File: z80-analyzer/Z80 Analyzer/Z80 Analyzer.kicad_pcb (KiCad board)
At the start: 2 copper layers, 65 x 65 mm, 49 parts, among them J1 Conn_01x40_Pin, M1 TestPoint, U1 Z80CPU

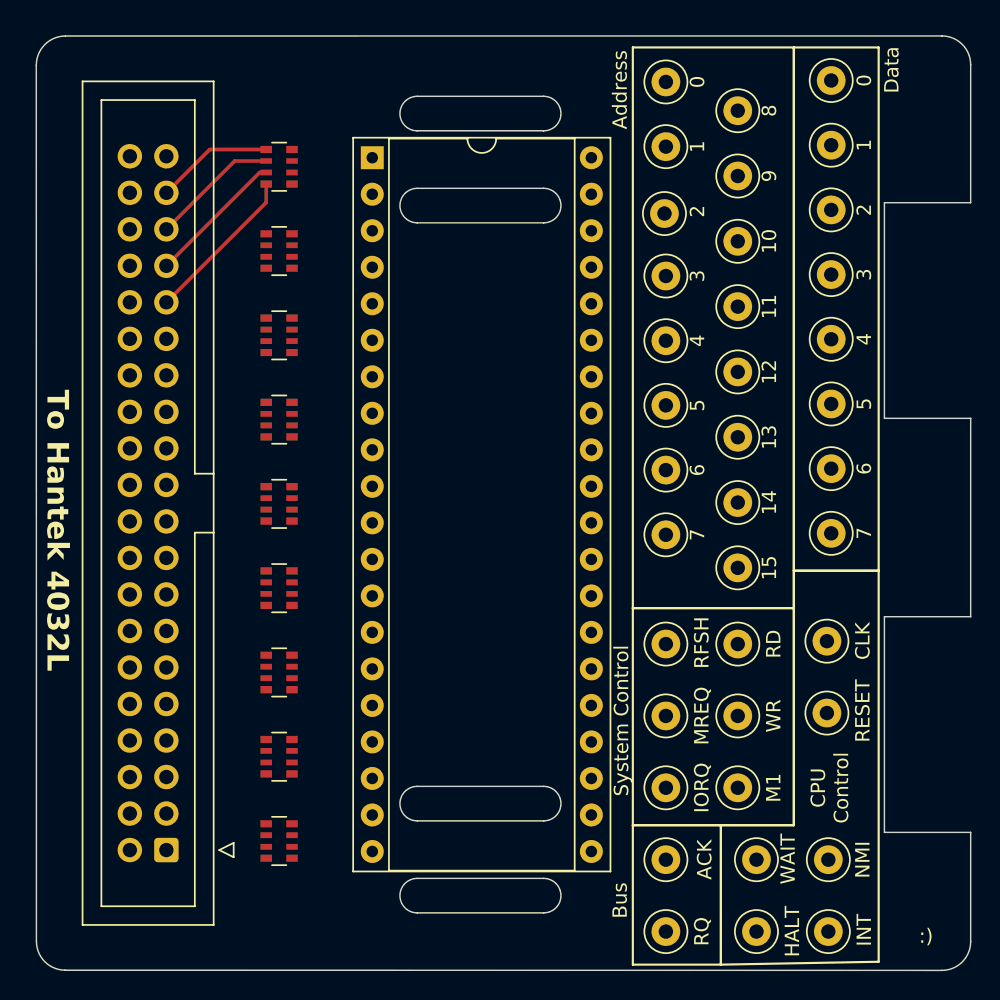
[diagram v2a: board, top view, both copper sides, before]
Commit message: [Z80] New routing, just needs rechecking now
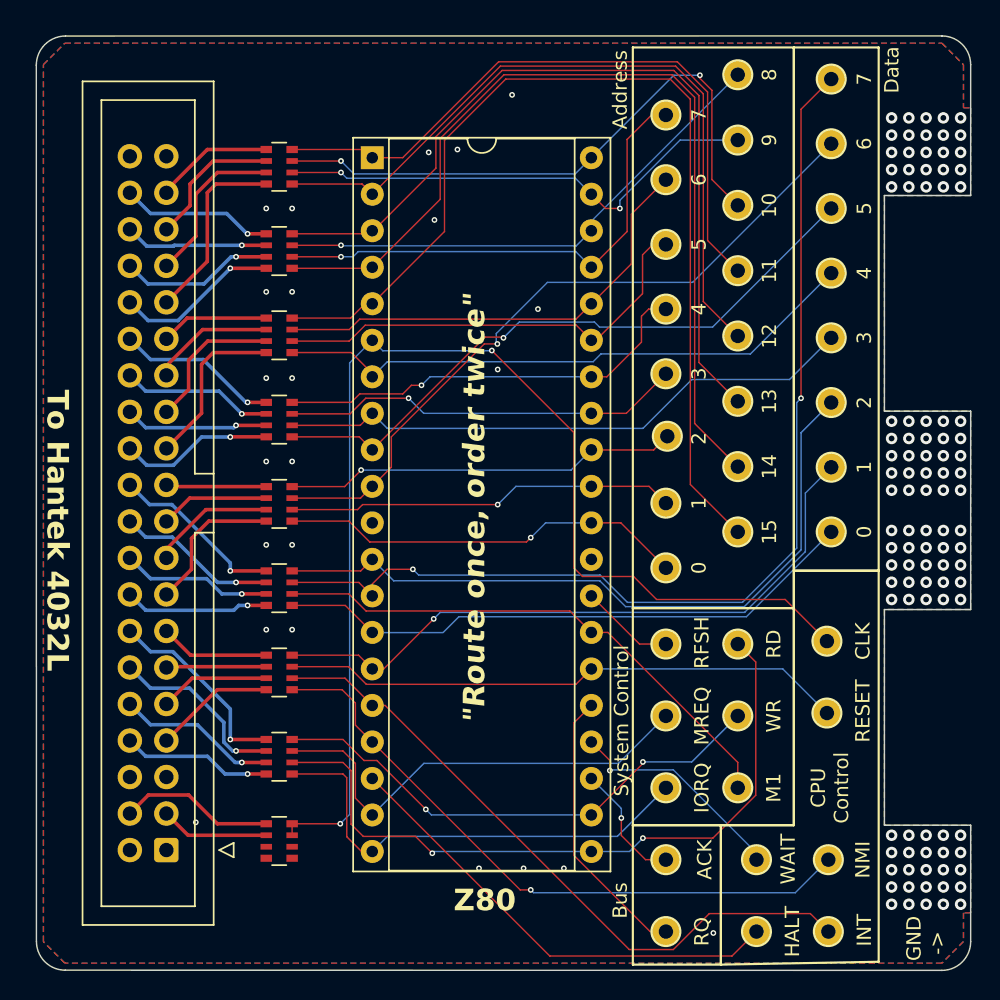
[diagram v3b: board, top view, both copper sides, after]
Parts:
- A0, A1, A10, A11, A12, A13, A14, A15, A2, A3, A4, A5, A6, A7, A8, A9, BUSACK1, BUSRQ1, CLK1, D0, D1, D2, D3, D4, D5, D6, D7, HALT1, INT1, IORQ1, M1, MREQ1, NMI1, RD1, RESET1, RFSH1, WAIT1, WR1: footprint TestPoint:TestPoint_Loop_D1.80mm_Drill1.0mm_Beaded -> CustomFootprints:TestPoint_Keystone_5021
- moved A0 33.8 mm to (165.0, 95.4), turned to -90 degrees
- moved D7 31.6 mm to (176.5, 61.4), turned to -90 degrees
- moved D0 31.4 mm to (176.5, 92.9), turned to -90 degrees
- moved A7 29.2 mm to (165.0, 63.9), turned to -90 degrees
- moved A1 24.8 mm to (165.0, 90.9), turned to -90 degrees
- moved D6 22.6 mm to (176.5, 65.9), turned to -90 degrees
- moved D1 22.4 mm to (176.5, 88.4), turned to -90 degrees
- moved A6 20.2 mm to (165.0, 68.4), turned to -90 degrees
- moved A2 15.5 mm to (165.1, 86.2), turned to -90 degrees
- moved D5 13.6 mm to (176.5, 70.4), turned to -90 degrees
- moved D2 13.4 mm to (176.5, 83.9), turned to -90 degrees
- moved A5 11.2 mm to (165.0, 72.9), turned to -90 degrees
- moved A3 6.80 mm to (165.0, 81.9), turned to -90 degrees
- moved D4 4.60 mm to (176.5, 74.9), turned to -90 degrees
- moved D3 4.40 mm to (176.5, 79.4), turned to -90 degrees
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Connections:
- RN1 pad 1: /S_A4 -> /S_A0
- RN1 pad 2: /S_A5 -> /S_A1
- RN1 pad 3: /S_A6 -> /S_D6
- RN1 pad 4: /S_A7 -> /S_A2
- RN2 pad 1: /S_A0 -> /S_NMI
- RN2 pad 2: /S_A1 -> /S_INT
- RN2 pad 3: /S_A2 -> /S_RESET
- RN2 pad 4: /S_A3 -> /S_D1
- RN3 pad 1: /S_A8 -> /S_D4
- RN3 pad 2: /S_A9 -> /S_A5
- RN3 pad 3: /S_A10 -> /S_A6
- RN3 pad 4: /S_A11 -> /S_A15
- RN4 pad 2: /S_A13 -> /S_A9
- RN4 pad 3: /S_A14 -> /S_A10
- RN4 pad 4: /S_A15 -> /S_A11
- RN5 pad 1: /S_D0 -> /S_IORQ
- RN5 pad 2: /S_D1 -> /S_RD
- RN5 pad 3: /S_D2 -> /S_MREQ
- RN5 pad 4: /S_D3 -> /S_WR
- RN6 pad 1: /S_D4 -> /S_D0
- RN6 pad 2: /S_D5 -> /S_M1
- RN6 pad 3: /S_D6 -> /S_D7
- RN6 pad 4: /S_D7 -> /S_D2
- RN7 pad 1: /S_WR -> /S_D5
- RN7 pad 2: /S_RD -> /S_D3
- RN7 pad 3: /S_IORQ -> /S_A3
- RN7 pad 4: /S_MREQ -> /S_A4
- RN8 pad 1: /S_RESET -> /S_A14
- RN8 pad 2: /S_M1 -> /S_A7
- RN8 pad 3: /S_INT -> /S_A8
- RN8 pad 4: /S_NMI -> /S_A13
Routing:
- net /S_CLK: track 0.00 -> 84.5 mm, vias 0 -> 2
- net /S_D7: track 0.00 -> 72.9 mm, vias 0 -> 2
- net /S_A15: track 0.00 -> 70.4 mm
- net /S_A14: track 0.00 -> 63.6 mm
- net /S_A13: track 0.00 -> 57.4 mm
- net /S_A12: track 0.00 -> 51.2 mm
- net /S_D2: track 0.00 -> 49.9 mm
- net /S_RD: track 0.00 -> 49.8 mm, vias 0 -> 2
- net /S_D6: track 0.00 -> 49.5 mm, vias 0 -> 1
- net /S_INT: track 0.00 -> 46.7 mm
- net /S_D1: track 0.00 -> 46.1 mm, vias 0 -> 1
- net /S_A11: track 0.00 -> 46.1 mm
- net /S_D5: track 0.00 -> 45.2 mm, vias 0 -> 1
- net /S_NMI: track 0.00 -> 45.0 mm, vias 0 -> 1
- net /S_A10: track 0.00 -> 41.7 mm, vias 0 -> 2
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- added copper zone on B.Cu, net GND
- added copper zone on F.Cu, net GND
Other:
- outline, holes or cut-outs redrawn
- board text added: "GND ->"
- board text added: "Z80"
- board text added: "{dblquote}Route once, order twice{dblquote}"
- board text removed: ":)"
